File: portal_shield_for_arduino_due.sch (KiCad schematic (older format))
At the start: 95 parts, among them J1 RS485_1, J10 ILLUM_SW_CONFIG, J2 ATX_PW_SW, J3 Sensor, J4 RS485_1_Config, J5 CAM_SW, J6 ILLUM_SW, J7 RS232_1, J8 RS232_2, J9 CAM_SW_CONFIG, K1 PA1A-12, P1 Power, P10 CONN_01X01, P11 CONN_01X01, P12 CONN_01X01, P13 CONN_01X01, P2 Analog, P3 Analog, P4 Digital, P5 PWM, P6 PWM, P7 Communication, P8 CONN_01X01, P9 CONN_01X01, Q1 BSS123LT1, Q10 FDN340P, Q11 FDN340P, Q2 STP16NF06L, Q3 STP16NF06L, Q4 FDN340P, Q5 FDN340P, Q6 FDN340P, Q7 FDN340P, Q8 FDN340P, Q9 FDN340P, SW1 SW_UART1, U1 LTV-817S, U2 LTV-817S, U3 MAX481E, U4 MP1584, U5 LTV-817S, U6 LTV-817S, U7 MAX3232

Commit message: Down-sizing with 2xrs232/rs485, and 2xinputs, and renamed into portal_shield_for_arduino_due
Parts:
- removed D2: 1N4148W, Diode_SMD:D_SOD-123, symbol Diode:1N4148W
- removed D3, D6: PW_SW_LED, LED_SMD:LED_0805_2012Metric, symbol Device:LED_ALT
- removed D5: CAM_SW_LED, LED_SMD:LED_0805_2012Metric, symbol Device:LED_ALT
- removed J1: RS485_1, TerminalBlock_Phoenix_PTSA:TerminalBlock_Phoenix_PTSA-1,5-4-3.5-Z_1x4_P3.5mm_Vertical, symbol Connector:Screw_Terminal_01x04
- removed J10: ILLUM_SW_CONFIG, Connector_PinHeader_2.54mm:PinHeader_2x03_P2.54mm_Vertical, symbol Connector_Generic:Conn_02x03_Odd_Even
- removed J2: ATX_PW_SW, TerminalBlock_Phoenix_PTSA:TerminalBlock_Phoenix_PTSA-1,5-2-3.5-Z_1x2_P3.5mm_Vertical, symbol Connector:Screw_Terminal_01x02
- removed J5: CAM_SW, TerminalBlock_Phoenix_PTSA:TerminalBlock_Phoenix_PTSA-1,5-2-3.5-Z_1x2_P3.5mm_Vertical, symbol Connector:Screw_Terminal_01x02
- removed J9: CAM_SW_CONFIG, Connector_PinHeader_2.54mm:PinHeader_2x03_P2.54mm_Vertical, symbol Connector_Generic:Conn_02x03_Odd_Even
- removed K1: PA1A-12, Relay_Panasonic:Relay_Panasonic_PA1a_xx_DIP, symbol portal_schematic-rescue:Relay_Panasonic_PA1a_XX_DIP-panasonic_pa_relays
- removed Q2, Q3: STP16NF06L, TO220_Heatsink:TO220_3_DH15A_HEATSINK, symbol Transistor_FET:IRLB8721PBF
- removed Q4, Q6, Q7: FDN340P, Package_TO_SOT_SMD:SOT-23, symbol Transistor_FET:Si2319CDS
- removed R23: 1K, Resistor_SMD:R_0805_2012Metric, symbol Device:R_US
- removed U1, U6: LTV-817S, Package_DIP:SMDIP-4_W9.53mm, symbol Isolator:LTV-817S
- added C12: 100n/50V, Capacitor_SMD:C_0805_2012Metric, symbol Device:C_Small
- added D2: ATX_SEN_LED, LED_SMD:LED_0805_2012Metric, symbol Device:LED_ALT
- added J1: RS485_1, TerminalBlock_Phoenix_PTSA:TerminalBlock_Phoenix_PTSA-1,5-3-3.5-Z_1x3_P3.5mm_Vertical, symbol Connector:Screw_Terminal_01x03
- added J2: RS485_2, TerminalBlock_Phoenix_PTSA:TerminalBlock_Phoenix_PTSA-1,5-3-3.5-Z_1x3_P3.5mm_Vertical, symbol Connector:Screw_Terminal_01x03
- added J5: RS485_2_Config, Connector_PinHeader_2.54mm:PinHeader_2x03_P2.54mm_Vertical, symbol Connector_Generic:Conn_02x03_Odd_Even
- added JP2: RS485_DIR2, Jumper:SolderJumper-3_P1.3mm_Open_Pad1.0x1.5mm, symbol Jumper:SolderJumper_3_Bridged12
- added Q2: BSS123LT1, Package_TO_SOT_SMD:SOT-23, symbol Transistor_FET:BSS138
- added Q3: FDN340P, Package_TO_SOT_SMD:SOT-23, symbol Transistor_FET:Si2319CDS
- added SW2: SW_UART2, Button_Switch_SMD:SW_CK_AYZ020AGRLC_DPDT_Straight, symbol Switch:SW_DPDT_x2
- added U1: MAX481E, Package_SO:SOIC-8_3.9x4.9mm_P1.27mm, symbol Interface_UART:MAX481E
- D4: value TICK_LED -> SYNC_LED
- J6: value ILLUM_SW -> ATX_SEN
- R11: value 1K -> 120
- R20: value 1K -> 10K
- R7: value 330 -> 1K
- U4: symbol portal_schematic-rescue:MP1584-MP1584 -> portal_shield_for_arduino_due-rescue:MP1584-MP1584-portal_schematic-rescue
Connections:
- net 24 is gone; now on net 24(ATX_SEN): P4.31 (Pin_31)
- net +5V: now also R1.1, R14.1, R20.1, C12.2, Q3.2 (S), U1.8 (VCC); no longer U5.4
- net 16(Tx2): now also SW2.2 (B); no longer U7.10 (T2IN)
- net 17(Rx2): now also SW2.5 (B); no longer U7.9 (R2OUT)
- net GND: now also R7.2, C12.1, D2.1 (K), J1.1 (Pin_1), J2.1 (Pin_1), Q2.2 (S), U1.5 (GND); no longer R14.1, U5.2
- net IOREF: now also U5.4
- net RS485_A1: now also J1.3 (Pin_3)
- net RS485_B1: now also J1.2 (Pin_2)
- net Vin(12V): no longer R7.1
- net at R1.2: now also J5.6 (Pin_6)
- net at R11.2: now also J5.4 (Pin_4); no longer U5.1
- net 24(ATX_SEN): now reaches U5.3
- net 24(ATX_SEN): now also R15.2, Q3.1 (G); no longer R14.2
- net RS485_TX2: now reaches R20.2
- net RS485_TX2: now also Q2.1 (G), SW2.1 (A), U1.4 (DI)
- net at J6.1 (Pin_1): now also U5.2
- net at J6.2 (Pin_2): now also R12.2
- net at R22.2: now also Q3.3 (D)
- net at R22.1: now also D2.2 (A)
- net 2(DIR1) renamed 2(**)
- net 2(**): no longer JP1.3 (B)
- net 22 renamed 22(DIR2)
- net 22(DIR2): now also JP2.3 (B)
- net 23 renamed 23(DIR1)
- net 23(DIR1): now also JP1.3 (B)
- net 25 renamed 25(SYNC)
- net 25(SYNC): now also Q5.1 (G), R8.2, U2.3
- net 3(PW_SW) renamed 3(**)
- net 3(**): no longer R1.1
- net 4(CAM_SW) renamed 4(**)
- net 4(**): no longer R11.1
- net 5(ILLUM_SW): no longer names the net of R12.1
- net 5(ILLUM_SW): now also U5.1; no longer P6.3 (Pin_3)
- removed net 6(TICK): P6.2 (Pin_2), Q5.1 (G), R8.2, U2.3
- new net: JP2.2 (C), U1.2 (~RE), U1.3 (DE)
- new net: J5.2 (Pin_2), R7.1
- new net 5(**): P6.3 (Pin_3)
- new net 6(**): P6.2 (Pin_2)
- new net AUTO_DIR2: JP2.1 (A), Q2.3 (D), R14.2
- new net RS232_TTL_RX2: SW2.6 (C), U7.9 (R2OUT)
- new net RS232_TTL_TX2: SW2.3 (C), U7.10 (T2IN)
- new net RS485_A2: J2.3 (Pin_3), J5.5 (Pin_5), R11.1, U1.6 (A)
- new net RS485_B2: J2.2 (Pin_2), J5.1 (Pin_1), J5.3 (Pin_3), U1.7 (B)
- new net RS485_RX2: SW2.4 (A), U1.1 (RO)
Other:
- note added: "ATX_POWER_MONITOR"
- note added: "OPTO_SENSOR"
- note added: "RS485_2"
- note removed: "ATX_POWER_SWITCH"
- note removed: "CAMERA_SWITCH\n"
- note removed: "ILLUMINATION_SWITCH"
- note removed: "OPTO_SENSOR_ISOLATOR"
- moved on the sheet: C1, C2, C4, C5, C6, C7, D1, D10, D11, D4, D7, D8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

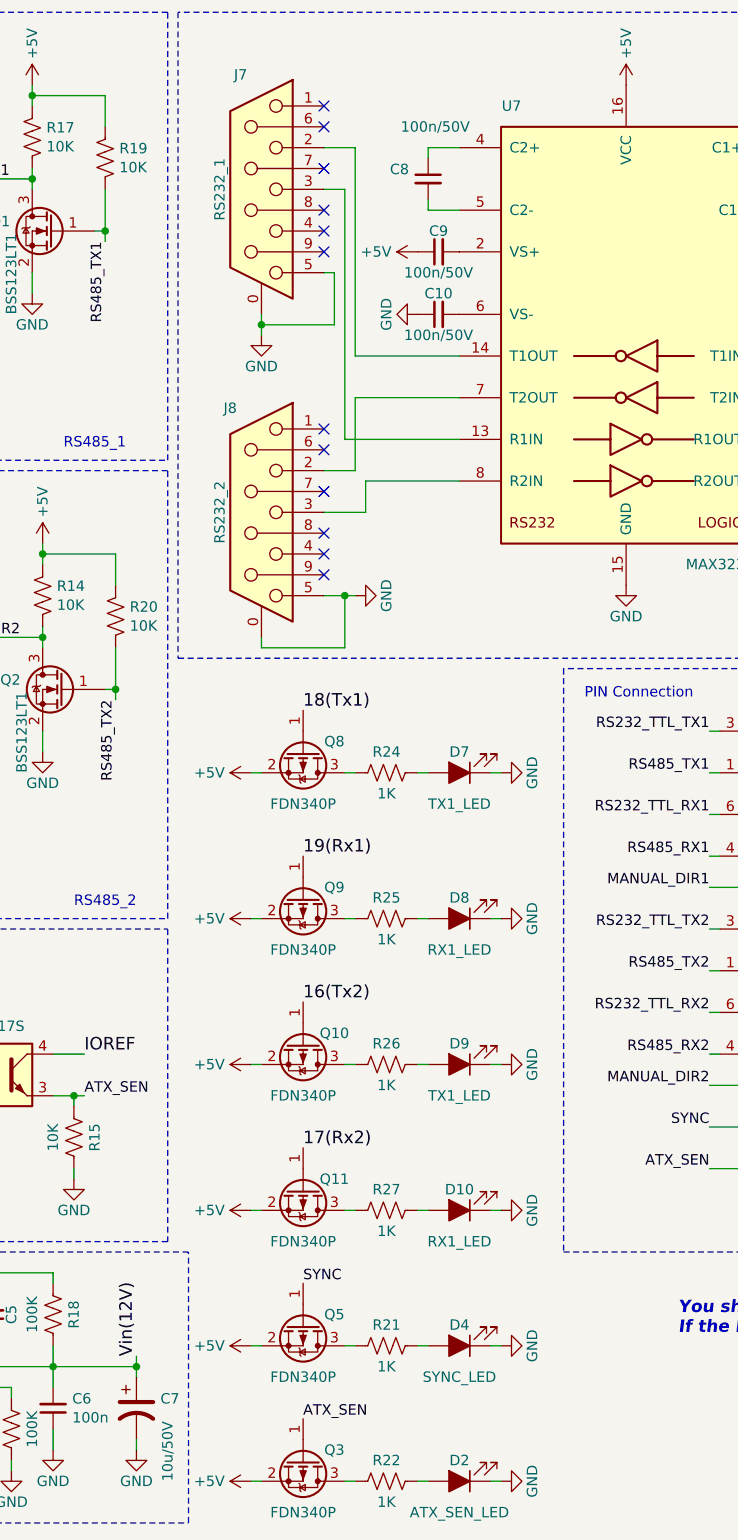
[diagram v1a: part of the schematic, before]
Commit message: modified to expand the interval between DSUB9s, and add labels of terminals
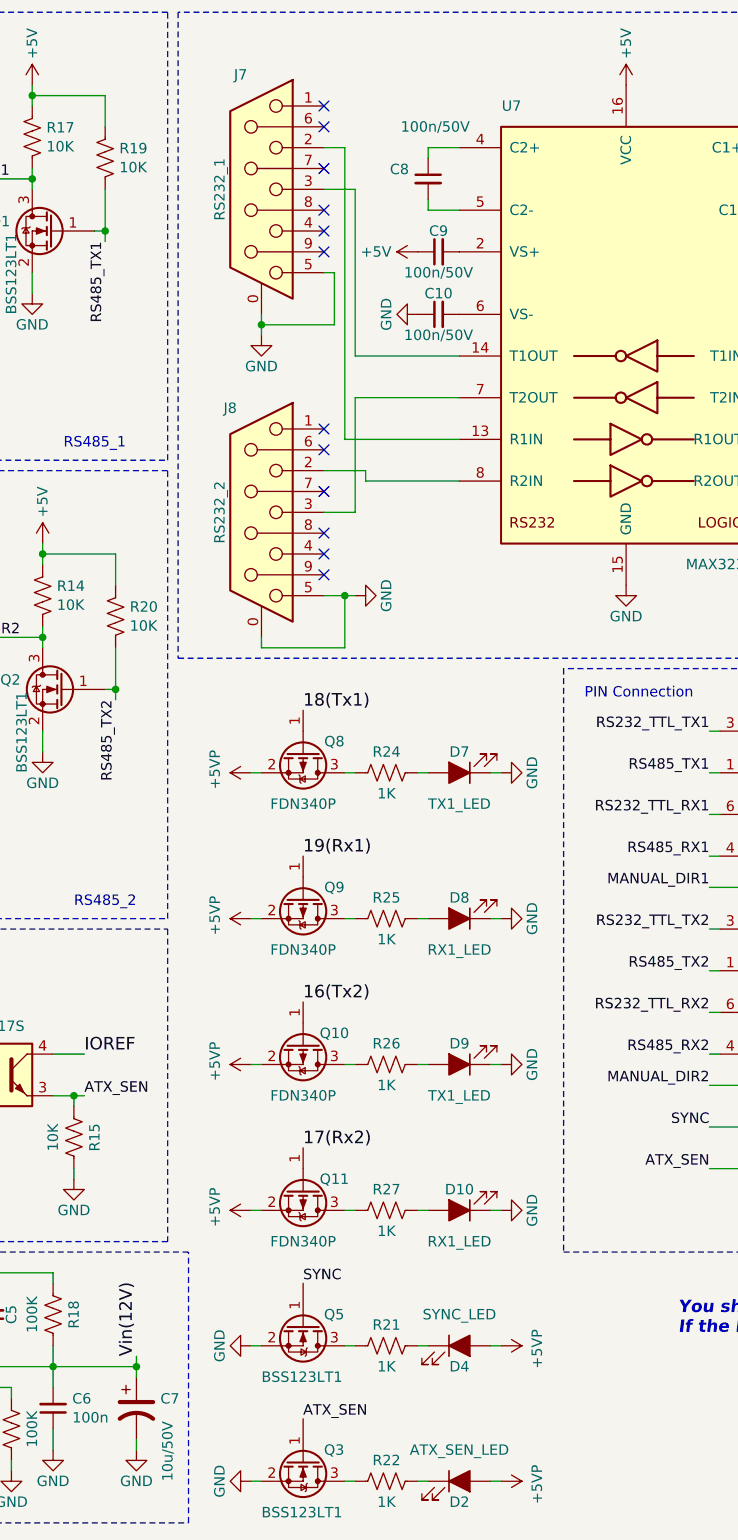
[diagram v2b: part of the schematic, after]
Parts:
- removed Q3, Q5: FDN340P, Package_TO_SOT_SMD:SOT-23, symbol Transistor_FET:Si2319CDS
- added Q3, Q5: BSS123LT1, Package_TO_SOT_SMD:SOT-23, symbol Transistor_FET:BSS138
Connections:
- net +5V: no longer Q10.2 (S), Q11.2 (S), Q8.2 (S), Q9.2 (S)
- net +5VP: now also D2.2 (A), D4.2 (A), Q10.2 (S), Q11.2 (S), Q8.2 (S), Q9.2 (S)
- net 24(ATX_SEN): now also Q3.1 (G)
- net 25(SYNC): now also Q5.1 (G)
- net GND: now also Q3.2 (S), Q5.2 (S); no longer D2.1 (K), D4.1 (K)
- net at J7.2: now also U7.13 (R1IN); no longer U7.14 (T1OUT)
- net at J7.3: now also U7.14 (T1OUT); no longer U7.13 (R1IN)
- net at J8.2: now also U7.8 (R2IN); no longer U7.7 (T2OUT)
- net at J8.3: now also U7.7 (T2OUT); no longer U7.8 (R2IN)
- net at R22.2: now also Q3.3 (D)
- net at R22.1: now also D2.1 (K); no longer D2.2 (A)
- net at R21.2: now also Q5.3 (D)
- net at R21.1: now also D4.1 (K); no longer D4.2 (A)
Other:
- moved on the sheet: D2, D4
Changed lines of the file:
@@
 	0    1    1    0
-$EndComp
-$Comp
-L power:+5V #PWR045
-U 1 1 5D5634FA
-P 5000 4150
-F 0 "#PWR045" H 5000 4000 50  0001 C CNN
-F 1 "+5V" V 5000 4350 50  0000 C CNN
-F 2 "" H 5000 4150 50  0000 C CNN
-F 3 "" H 5000 4150 50  0000 C CNN
-	1    5000 4150
-	0    -1   -1   0
 $EndComp
 Wire Wire Line
@@
 	-1   0    0    1
 $EndComp
-$Comp
-L power:GND #PWR049
-U 1 1 5D5BD9CF
-P 6200 4150
-F 0 "#PWR049" H 6200 3900 50  0001 C CNN
-F 1 "GND" H 6200 4000 50  0000 C CNN
-F 2 "" H 6200 4150 50  0000 C CNN
-F 3 "" H 6200 4150 50  0000 C CNN
-	1    6200 4150
-	0    -1   -1   0
-$EndComp
 Wire Wire Line
 	6200 4150 6150 4150
@@
 	0    1    1    0
 $EndComp
-$Comp
-L power:+5V #PWR046
-U 1 1 5D60DB78
-P 5000 4850
-F 0 "#PWR046" H 5000 4700 50  0001 C CNN
-F 1 "+5V" V 5000 5050 50  0000 C CNN
-F 2 "" H 5000 4850 50  0000 C CNN
-F 3 "" H 5000 4850 50  0000 C CNN
-	1    5000 4850
-	0    -1   -1   0
-$EndComp
 Wire Wire Line
 	5000 4850 5050 4850
@@
 	-1   0    0    1
 $EndComp
-$Comp
-L power:GND #PWR050
-U 1 1 5D60DB8D
-P 6200 4850
-F 0 "#PWR050" H 6200 4600 50  0001 C CNN
-F 1 "GND" H 6200 4700 50  0000 C CNN
-F 2 "" H 6200 4850 50  0000 C CNN
-F 3 "" H 6200 4850 50  0000 C CNN
-	1    6200 4850
-	0    -1   -1   0
-$EndComp
 Wire Wire Line
 	6200 4850 6150 4850
@@
 	0    1    1    0
 $EndComp
-$Comp
-L power:+5V #PWR047
-U 1 1 5D6C77DD
-P 5000 5550
-F 0 "#PWR047" H 5000 5400 50  0001 C CNN
-F 1 "+5V" V 5000 5750 50  0000 C CNN
-F 2 "" H 5000 5550 50  0000 C CNN
-F 3 "" H 5000 5550 50  0000 C CNN
-	1    5000 5550
-	0    -1   -1   0
-$EndComp
 Wire Wire Line
 	5000 5550 5050 5550
@@
 	-1   0    0    1
 $EndComp
-$Comp
-L power:GND #PWR051
-U 1 1 5D6C77F2
-P 6200 5550
-F 0 "#PWR051" H 6200 5300 50  0001 C CNN
-F 1 "GND" H 6200 5400 50  0000 C CNN
-F 2 "" H 6200 5550 50  0000 C CNN
-F 3 "" H 6200 5550 50  0000 C CNN
-	1    6200 5550
-	0    -1   -1   0
-$EndComp
 Wire Wire Line
 	6200 5550 6150 5550
@@
 	0    1    1    0
 $EndComp
-$Comp
-L power:+5V #PWR048
-U 1 1 5D6C7805
-P 5000 6250
-F 0 "#PWR048" H 5000 6100 50  0001 C CNN
-F 1 "+5V" V 5000 6450 50  0000 C CNN
-F 2 "" H 5000 6250 50  0000 C CNN
-F 3 "" H 5000 6250 50  0000 C CNN
-	1    5000 6250
-	0    -1   -1   0
-$EndComp
 Wire Wire Line
 	5000 6250 5050 6250
@@
 	1    6000 6250
 	-1   0    0    1
-$EndComp
-$Comp
-L power:GND #PWR052
-U 1 1 5D6C781A
-P 6200 6250
-F 0 "#PWR052" H 6200 6000 50  0001 C CNN
-F 1 "GND" H 6200 6100 50  0000 C CNN
-F 2 "" H 6200 6250 50  0000 C CNN
-F 3 "" H 6200 6250 50  0000 C CNN
-	1    6200 6250
-	0    -1   -1   0
 $EndComp
 Wire Wire Line
@@
 	4600 500  550  500
 Wire Wire Line
-	5350 2900 5550 2900
-Wire Wire Line
-	5550 2900 5550 2750
-Wire Wire Line
-	5550 2750 6000 2750
-Wire Wire Line
-	6000 2350 5500 2350
-Wire Wire Line
-	5500 2350 5500 2700
-Wire Wire Line
-	5500 2700 5350 2700
-Wire Wire Line
 	5050 3550 5450 3550
 Wire Wire Line
@@
 Wire Wire Line
 	5050 2000 5050 2050
-Wire Wire Line
-	5350 1150 5500 1150
-Wire Wire Line
-	5500 1150 5500 2150
-Wire Wire Line
-	5500 2150 6000 2150
-Wire Wire Line
-	5450 1350 5450 2550
-Wire Wire Line
-	5450 2550 6000 2550
-Wire Wire Line
-	5350 1350 5450 1350
 Wire Notes Line
 	4650 500  4650 3600
@@
 	-1   0    0    -1
 $EndComp
-$Comp
-L Transistor_FET:Si2319CDS Q5
-U 1 1 5D212CED
-P 5250 6800
-F 0 "Q5" V 5200 6950 50  0000 C CNN
-F 1 "FDN340P" V 5500 6800 50  0000 C CNN
-F 2 "Package_TO_SOT_SMD:SOT-23" H 5450 6725 50  0001 L CIN
-F 3 "http://www.vishay.com/docs/66709/si2319cd.pdf" H 5250 6800 50  0001 L CNN
-	1    5250 6800
-	0    1    1    0
-$EndComp
-$Comp
-L power:+5V #PWR033
-U 1 1 5D212CF4
-P 5000 6900
-F 0 "#PWR033" H 5000 6750 50  0001 C CNN
-F 1 "+5V" V 5000 7100 50  0000 C CNN
-F 2 "" H 5000 6900 50  0000 C CNN
-F 3 "" H 5000 6900 50  0000 C CNN
-	1    5000 6900
-	0    -1   -1   0
-$EndComp
 Wire Wire Line
 	5000 6900 5050 6900
@@
 F 3 "~" H 6000 6900 50  0001 C CNN
 	1    6000 6900
-	-1   0    0    1
-$EndComp
-$Comp
-L power:GND #PWR040
-U 1 1 5D212D09
-P 6200 6900
-F 0 "#PWR040" H 6200 6650 50  0001 C CNN
-F 1 "GND" H 6200 6750 50  0000 C CNN
-F 2 "" H 6200 6900 50  0000 C CNN
-F 3 "" H 6200 6900 50  0000 C CNN
-	1    6200 6900
-	0    -1   -1   0
+	1    0    0    -1
 $EndComp
 Wire Wire Line
@@
 Wire Notes Line
 	4700 6450 550  6450
-$Comp
-L Transistor_FET:Si2319CDS Q3
-U 1 1 5D04EF82
-P 5250 7450
-F 0 "Q3" V 5200 7600 50  0000 C CNN
-F 1 "FDN340P" V 5500 7450 50  0000 C CNN
-F 2 "Package_TO_SOT_SMD:SOT-23" H 5450 7375 50  0001 L CIN
-F 3 "http://www.vishay.com/docs/66709/si2319cd.pdf" H 5250 7450 50  0001 L CNN
-	1    5250 7450
-	0    1    1    0
-$EndComp
-$Comp
-L power:+5V #PWR032
-U 1 1 5D04EF88
-P 5000 7550
-F 0 "#PWR032" H 5000 7400 50  0001 C CNN
-F 1 "+5V" V 5000 7750 50  0000 C CNN
-F 2 "" H 5000 7550 50  0000 C CNN
-F 3 "" H 5000 7550 50  0000 C CNN
-	1    5000 7550
-	0    -1   -1   0
-$EndComp
 Wire Wire Line
 	5000 7550 5050 7550
@@
 F 3 "~" H 6000 7550 50  0001 C CNN
 	1    6000 7550
-	-1   0    0    1
+	1    0    0    -1
 $EndComp
 $Comp
 L power:GND #PWR034
 U 1 1 5D04EF9B
-P 6200 7550
-F 0 "#PWR034" H 6200 7300 50  0001 C CNN
-F 1 "GND" H 6200 7400 50  0000 C CNN
-F 2 "" H 6200 7550 50  0000 C CNN
-F 3 "" H 6200 7550 50  0000 C CNN
-	1    6200 7550
-	0    -1   -1   0
+P 5000 6900
+F 0 "#PWR034" H 5000 6650 50  0001 C CNN
+F 1 "GND" H 5000 6750 50  0000 C CNN
+F 2 "" H 5000 6900 50  0000 C CNN
+F 3 "" H 5000 6900 50  0000 C CNN
+	1    5000 6900
+	0    1    1    0
 $EndComp
 Wire Wire Line
@@
 Text Label 5250 7250 0    50   ~ 0
 ATX_SEN
+$Comp
+L power:GND #PWR?
+U 1 1 5D334F72
+P 6200 6250
+F 0 "#PWR?" H 6200 6000 50  0001 C CNN
+F 1 "GND" H 6200 6100 50  0000 C CNN
+F 2 "" H 6200 6250 50  0000 C CNN
+F 3 "" H 6200 6250 50  0000 C CNN
+	1    6200 6250
+	0    -1   -1   0
+$EndComp
+$Comp
+L power:GND #PWR?
+U 1 1 5D3353B3
+P 6200 5550
+F 0 "#PWR?" H 6200 5300 50  0001 C CNN
+F 1 "GND" H 6200 5400 50  0000 C CNN
+F 2 "" H 6200 5550 50  0000 C CNN
+F 3 "" H 6200 5550 50  0000 C CNN
+	1    6200 5550
+	0    -1   -1   0
+$EndComp
+$Comp
+L power:GND #PWR?
+U 1 1 5D335470
+P 6200 4850
+F 0 "#PWR?" H 6200 4600 50  0001 C CNN
+F 1 "GND" H 6200 4700 50  0000 C CNN
+F 2 "" H 6200 4850 50  0000 C CNN
+F 3 "" H 6200 4850 50  0000 C CNN
+	1    6200 4850
+	0    -1   -1   0
+$EndComp
+$Comp
+L power:GND #PWR?
+U 1 1 5D3357F5
+P 6200 4150
+F 0 "#PWR?" H 6200 3900 50  0001 C CNN
+F 1 "GND" H 6200 4000 50  0000 C CNN
+F 2 "" H 6200 4150 50  0000 C CNN
+F 3 "" H 6200 4150 50  0000 C CNN
+	1    6200 4150
+	0    -1   -1   0
+$EndComp
+$Comp
+L power:GND #PWR?
+U 1 1 5D45A46E
+P 5000 7550
+F 0 "#PWR?" H 5000 7300 50  0001 C CNN
+F 1 "GND" H 5000 7400 50  0000 C CNN
+F 2 "" H 5000 7550 50  0000 C CNN
+F 3 "" H 5000 7550 50  0000 C CNN
+	1    5000 7550
+	0    1    1    0
+$EndComp
+$Comp
+L Transistor_FET:BSS138 Q5
+U 1 1 5D45ABC6
+P 5250 6800
+F 0 "Q5" V 5200 6900 50  0000 L CNN
+F 1 "BSS123LT1" V 5500 6600 50  0000 L CNN
+F 2 "Package_TO_SOT_SMD:SOT-23" H 5450 6725 50  0001 L CIN
+F 3 "https://www.fairchildsemi.com/datasheets/BS/BSS138.pdf" H 5250 6800 50  0001 L CNN
+	1    5250 6800
+	0    1    1    0
+$EndComp
+$Comp
+L Transistor_FET:BSS138 Q3
+U 1 1 5D480310
+P 5250 7450
+F 0 "Q3" V 5200 7550 50  0000 L CNN
+F 1 "BSS123LT1" V 5500 7250 50  0000 L CNN
+F 2 "Package_TO_SOT_SMD:SOT-23" H 5450 7375 50  0001 L CIN
+F 3 "https://www.fairchildsemi.com/datasheets/BS/BSS138.pdf" H 5250 7450 50  0001 L CNN
+	1    5250 7450
+	0    1    1    0
+$EndComp
+$Comp
+L power:+5VP #PWR?
+U 1 1 5D520134
+P 6200 6900
+F 0 "#PWR?" H 6200 6750 50  0001 C CNN
+F 1 "+5VP" H 6215 7073 50  0000 C CNN
+F 2 "" H 6200 6900 50  0001 C CNN
+F 3 "" H 6200 6900 50  0001 C CNN
+	1    6200 6900
+	0    1    1    0
+$EndComp
+$Comp
+L power:+5VP #PWR?
+U 1 1 5D520E1C
+P 5000 4150
+F 0 "#PWR?" H 5000 4000 50  0001 C CNN
+F 1 "+5VP" H 5015 4323 50  0000 C CNN
+F 2 "" H 5000 4150 50  0001 C CNN
+F 3 "" H 5000 4150 50  0001 C CNN
+	1    5000 4150
+	0    -1   -1   0
+$EndComp
+$Comp
+L power:+5VP #PWR?
+U 1 1 5D521148
+P 5000 4850
+F 0 "#PWR?" H 5000 4700 50  0001 C CNN
+F 1 "+5VP" H 5015 5023 50  0000 C CNN
+F 2 "" H 5000 4850 50  0001 C CNN
+F 3 "" H 5000 4850 50  0001 C CNN
+	1    5000 4850
+	0    -1   -1   0
+$EndComp
+$Comp
+L power:+5VP #PWR?
+U 1 1 5D521205
+P 5000 5550
+F 0 "#PWR?" H 5000 5400 50  0001 C CNN
+F 1 "+5VP" H 5015 5723 50  0000 C CNN
+F 2 "" H 5000 5550 50  0001 C CNN
+F 3 "" H 5000 5550 50  0001 C CNN
+	1    5000 5550
+	0    -1   -1   0
+$EndComp
+$Comp
+L power:+5VP #PWR?
+U 1 1 5D5212C2
+P 5000 6250
+F 0 "#PWR?" H 5000 6100 50  0001 C CNN
+F 1 "+5VP" H 5015 6423 50  0000 C CNN
+F 2 "" H 5000 6250 50  0001 C CNN
+F 3 "" H 5000 6250 50  0001 C CNN
+	1    5000 6250
+	0    -1   -1   0
+$EndComp
+$Comp
+L power:+5VP #PWR?
+U 1 1 5D5225F8
+P 6200 7550
+F 0 "#PWR?" H 6200 7400 50  0001 C CNN
+F 1 "+5VP" H 6215 7723 50  0000 C CNN
+F 2 "" H 6200 7550 50  0001 C CNN
+F 3 "" H 6200 7550 50  0001 C CNN
+	1    6200 7550
+	0    1    1    0
+$EndComp
+Wire Wire Line
+	5350 1350 5500 1350
+Wire Wire Line
+	5500 1350 5500 2150
+Wire Wire Line
+	5500 2150 6000 2150
+Wire Wire Line
+	5350 1150 5450 1150
+Wire Wire Line
+	5450 1150 5450 2550
+Wire Wire Line
+	5450 2550 6000 2550
+Wire Wire Line
+	5350 2700 5550 2700
+Wire Wire Line
+	5550 2700 5550 2750
+Wire Wire Line
+	5550 2750 6000 2750
+Wire Wire Line
+	6000 2350 5500 2350
+Wire Wire Line
+	5500 2350 5500 2900
+Wire Wire Line
+	5500 2900 5350 2900
 $EndSCHEMATC
